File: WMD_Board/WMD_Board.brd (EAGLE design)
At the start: 65 x 45 mm, 60 parts, among them IC1 FGPMMOPA6H, J1 EMPCB.SMAFSTJ.B.HT, Q1 SI2323DS-T1-E3, U1 STM32L053C8T6, U2 BSS138, U3 RFM69HCW, U4 BSS138, U6 TPS72218DBVR, U7 M24512-DRMN8TP/K, Y2 ABS06-107-32.768KHZ-T

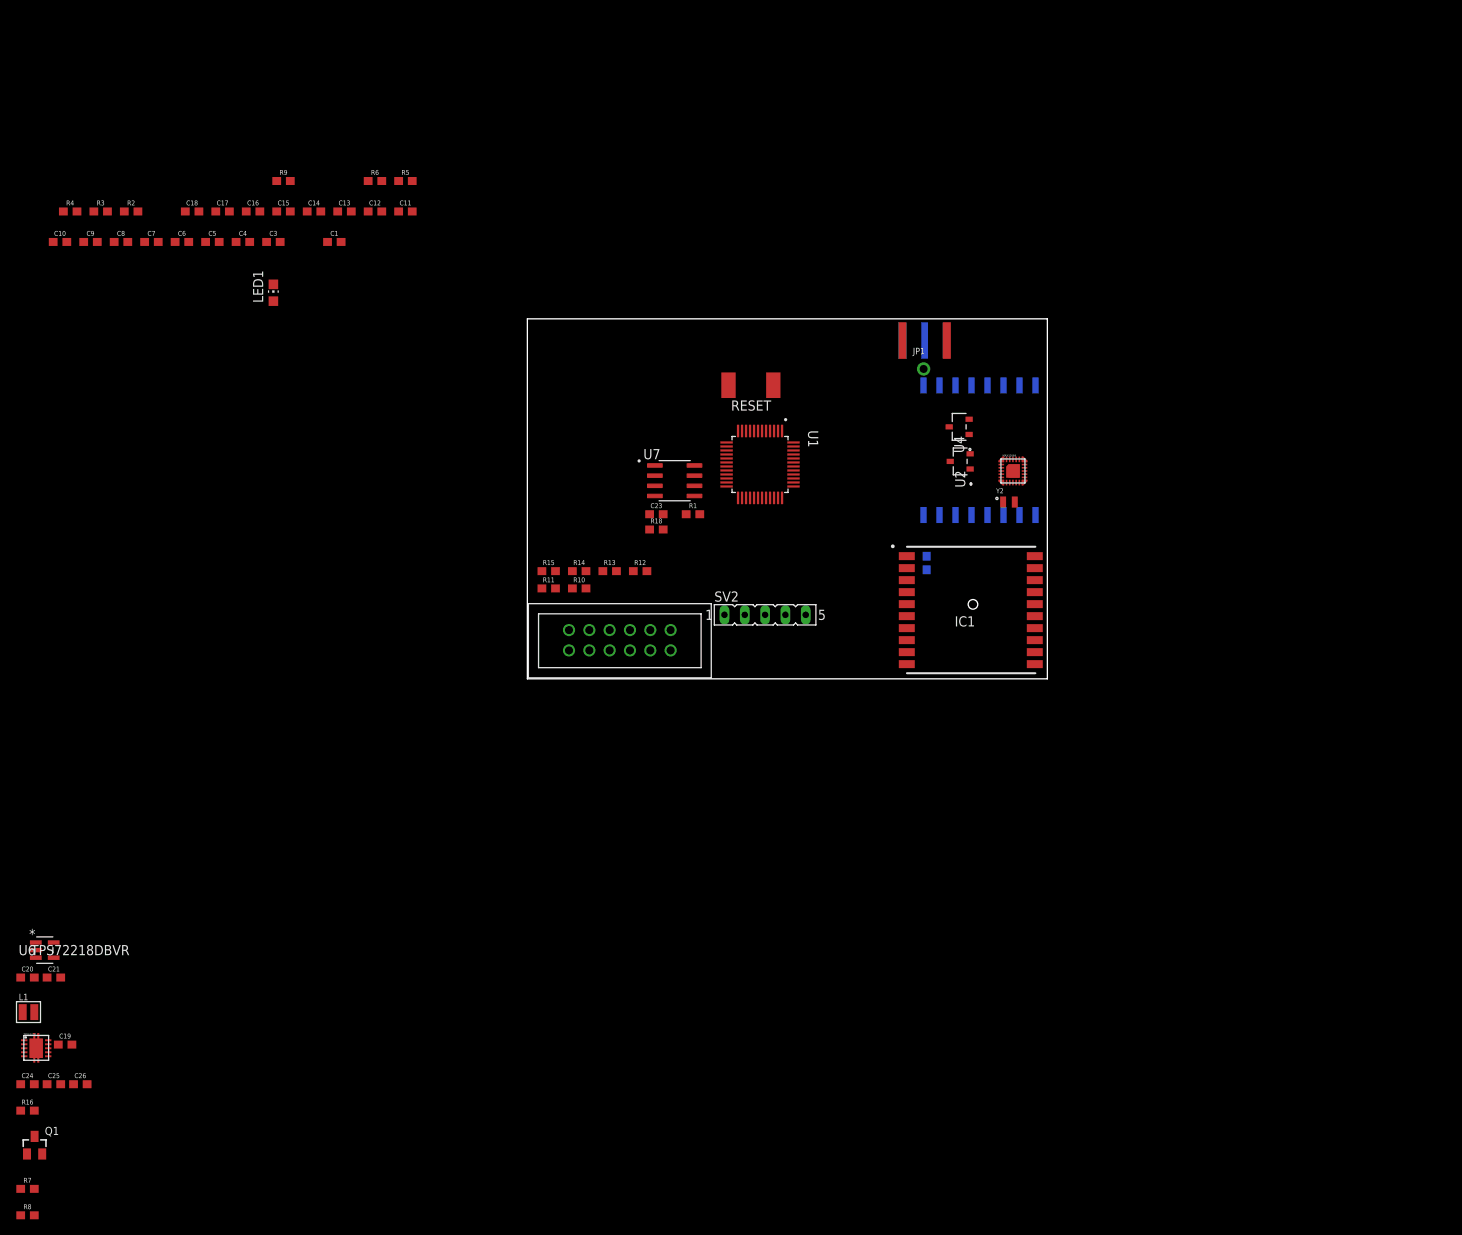
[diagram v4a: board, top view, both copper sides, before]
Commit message: Board routing started
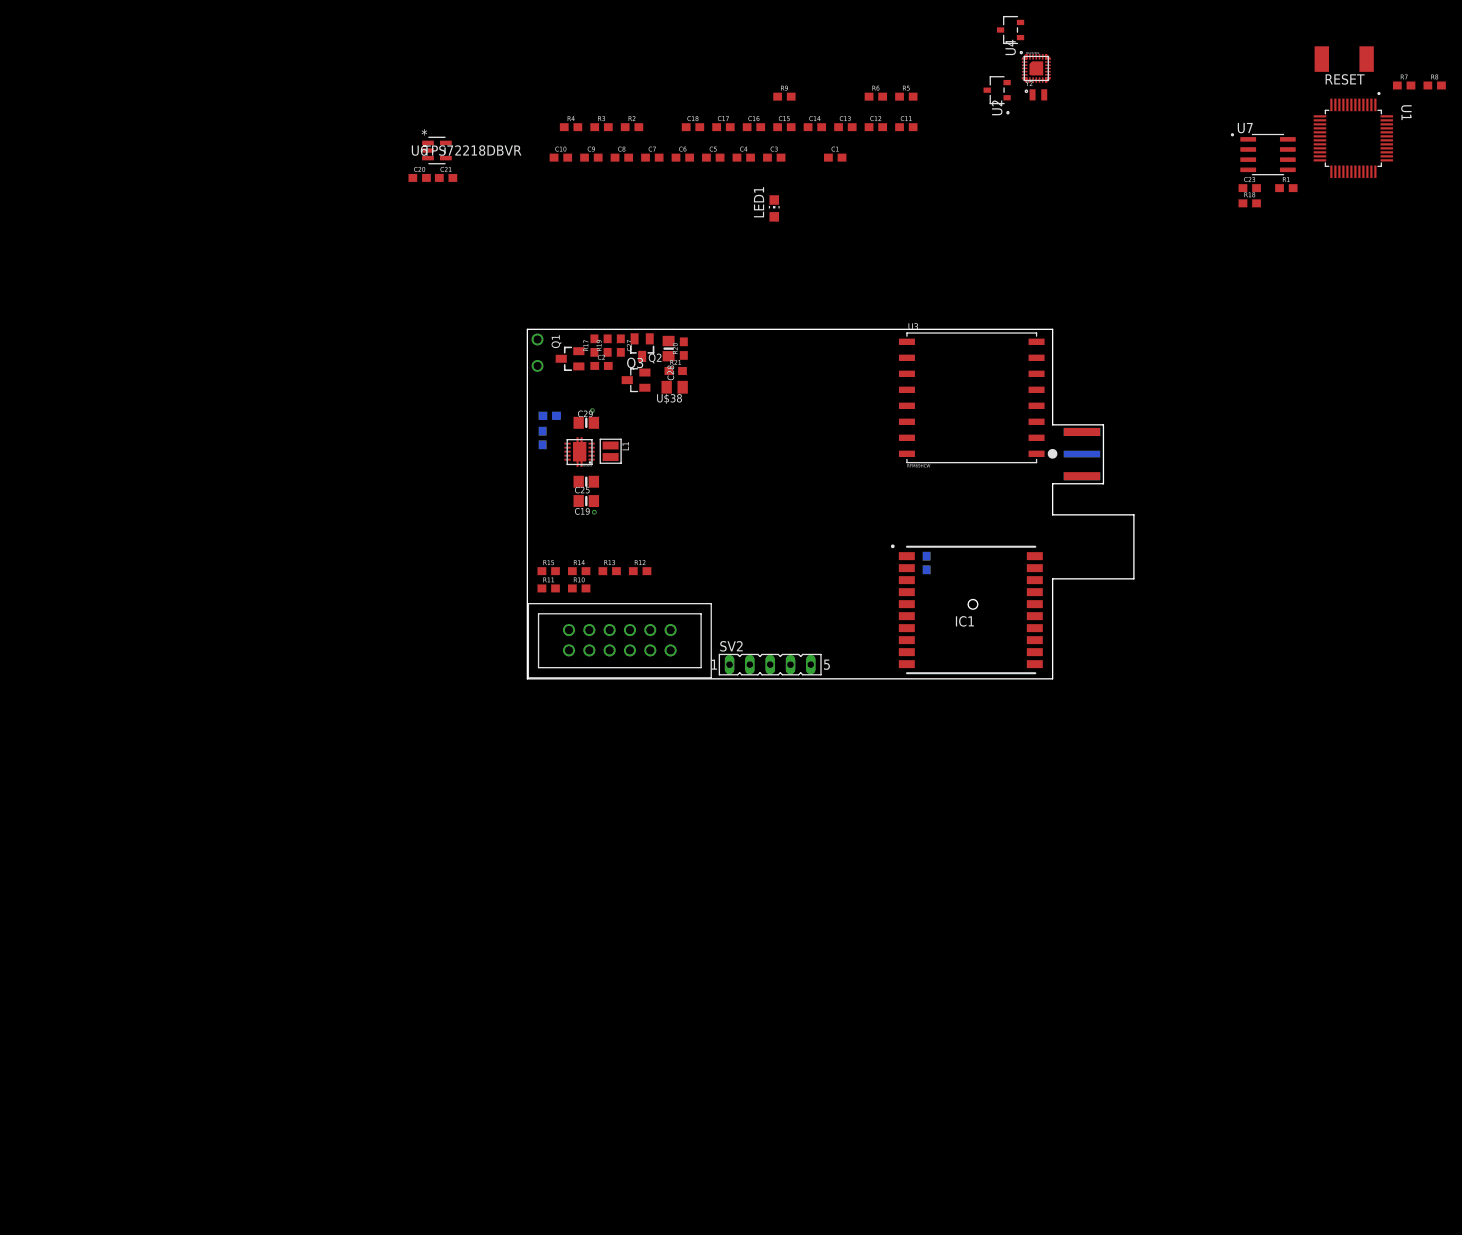
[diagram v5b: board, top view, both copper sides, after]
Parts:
- removed C24: 10uF, SparkFun-Capacitors:0603
- removed JP1: (no value), microbuilder:1X01_ROUND
- added C2, C27: 1.0uF, SparkFun-Capacitors:0603
- added C28, C29: 10uF, microbuilder:0805-NO
- added Q2: SI2323DS-T1-E3, SI2323DS-T1-E3:SOT23
- added Q3: SI2312BDS, SI2312BDS:SOT23
- added R17, R19, R20, R21: 1k, SparkFun-Resistors:0603
- added U$38: TS4148C_RZG, TS4148_RY:C0805K
- added U$40, U$41: BATTERY_HOLE, Battery_Hole:BATTERY_HOLE
- C11, C13, C18: value 1uF -> 1.0uF
- C14: value 100nF -> 1.0uF
- C17: value 0.1uF -> 4.7uF
- C19, C25: device SparkFun-Capacitors:0603 -> microbuilder:0805-NO
- C22: value 0.1uF -> 10uF
- R1, R18, R4, R5, R6, R9: value 4.7k -> 1k
- R16: value 100 -> 1k
- R3: value 10 -> 100k
- R7, R8: value 100k -> 1k
- moved R8 225.6 mm to (113.4, 74.2)
- moved R7 220.5 mm to (109.6, 74.2)
- moved Q1 118.9 mm to (5.33, 40.0), turned to 90 degrees
- moved U6 111.3 mm to (-11.3, 66.0)
- moved C20 111.3 mm to (-13.5, 62.6)
- moved C21 111.3 mm to (-10.2, 62.6)
- moved R16 108.7 mm to (2.79, 32.9), flipped to the bottom, turned to 180 degrees
- moved U$22 105.5 mm to (8.13, 30.1), turned to 180 degrees
- moved L1 101.0 mm to (10.4, 28.4), turned to 270 degrees
- moved C25 100.5 mm to (7.37, 24.6), turned to 180 degrees
- moved C26 99.3 mm to (1.91, 30.1), flipped to the bottom, turned to 270 degrees
- moved C19 94.1 mm to (7.37, 22.2), turned to 180 degrees
- moved R1 84.6 mm to (94.9, 61.3)
- moved RESET 84.6 mm to (102.1, 77.5)
- moved U1 84.6 mm to (103.3, 67.6)
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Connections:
- removed net V_BAT_MEASURE: R7.1
- new net MEASURE: C27.1, Q1.2, Q2.2, R17.2, R19.2, R7.1
- new net N$13: C28.2, Q3.1, R21.1
- new net N$14: C2.2, C27.2, Q2.1, Q3.3, R19.1
- new net SHUTDOWN: R20.1, R21.2, U$38.A, U1.2
- net 3.3V: now also C25.1; no longer C24.1
- net BTN_POWER_OUT: now also C2.1, R17.1, U$38.C
- net GND: now also C29.2, Q3.2, U$41.1; no longer C24.2
- net N$8: no longer JP1.1
- net VIN_BATTERY: now also U$40.1
- net VIN_BB: now also C28.1, C29.1, Q2.3, R20.2; no longer C25.1
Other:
- board size 65 x 45 mm -> 75.8 x 43.7 mm

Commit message: lots of routing stuff
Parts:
- added C24: 0.01uF, SparkFun-Capacitors:0603
- added C30: 0.1uF, SparkFun-Capacitors:0603
- added J2: 5015680607, WMD_TO_HRF:MOLEX_5015680607
- R4, R5, R6, R9: value 1k -> 4.7k
- moved RESET 125.4 mm to (-16.6, 37.2), turned to 0 degrees
- moved U1 101.9 mm to (12.1, 22.1)
- moved U7 99.7 mm to (3.43, 21.0), turned to 270 degrees
- moved U2 96.7 mm to (-16.9, 13.2)
- moved C20 93.2 mm to (79.3, 54.1), flipped to the bottom
- moved C21 92.7 mm to (81.8, 51.1), flipped to the bottom, turned to 90 degrees
- moved C23 92.0 mm to (4.06, 29.2), flipped to the bottom
- moved U6 91.7 mm to (79.2, 51.2), flipped to the bottom, turned to 90 degrees
- moved R5 87.5 mm to (-18.8, 15.6), turned to 270 degrees
- moved R1 81.8 mm to (20.7, 26.8), turned to 180 degrees
- moved R18 77.1 mm to (21.2, 25.3), turned to 180 degrees
- moved U4 73.0 mm to (40.5, 10.9)
- moved C5 64.3 mm to (13.7, 1.52), flipped to the bottom, turned to 180 degrees
- moved C4 63.5 mm to (2.29, 6.73), flipped to the bottom
- moved R6 63.3 mm to (36.8, 9.87)
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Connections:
- removed net BTN_2_2: C3.2
- removed net BTN_3_2: C4.2
- removed net BTN_4_2: C5.2
- net 1.8V: now also J2.1
- net 3.3V: now also C24.1, C30.1, J2.3
- net GND: now also C24.2, C3.2, C30.2, C4.2, C5.2, J2.6
- net INT: now also J2.2
- net SCL_TO_HR_SENSOR: now also J2.5
- net SDA_TO_HR_SENSOR: now also J2.4
- net WC_EEPROM: now also U1.20; no longer U1.46
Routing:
- net 3.3V: track 0.00 -> 19.6 mm, vias 0 -> 4
- net VIN_BB: track 0.00 -> 12.2 mm, vias 0 -> 2
- net N$14: track 0.00 -> 11.8 mm
- net MEASURE: track 0.00 -> 7.99 mm
- net N$13: track 0.00 -> 6.60 mm
- net N$8: track 0.00 -> 5.71 mm
- net GND: track 0.00 -> 5.06 mm
- net N$7: track 0.00 -> 4.76 mm
- net VIN_BATTERY: track 0.00 -> 4.22 mm
- net SHUTDOWN: track 0.00 -> 4.14 mm
- added copper zone on layer 1, net 3.3V
- added copper zone on layer 1, net GND
- added copper zone on layer 16, net GND
- added copper zone on layer 1, net N$2
- added copper zone on layer 1, net N$3
- added copper zone on layer 1, net VIN_BB
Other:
- board size 75.8 x 43.7 mm -> 75.7 x 43.7 mm

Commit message: lots of routing stuff
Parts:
- moved C30 1.27 mm to (35.4, 38.1)
- moved C24 1.27 mm to (37.0, 38.1)
- moved C19 1.02 mm to (32.8, 38.0)
- moved C25 0.51 mm to (30.9, 38.0)
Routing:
- net 3.3V: track 19.6 -> 18.3 mm
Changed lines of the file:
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@@
 <attribute name="VALUE" x="23.241" y="35.941" size="0.4064" layer="27" ratio="10" rot="R270"/>
 </element>
-<element name="C25" library="microbuilder" package="0805-NO" value="10uF" x="31.369" y="37.973" smashed="yes" rot="R270">
-<attribute name="NAME" x="32.004" y="38.481" size="0.8128" layer="25" ratio="18" rot="R270"/>
-<attribute name="VALUE" x="30.607" y="35.941" size="0.4064" layer="27" ratio="10" rot="R270"/>
-</element>
-<element name="C19" library="microbuilder" package="0805-NO" value="10uF" x="33.782" y="37.973" smashed="yes" rot="R270">
-<attribute name="NAME" x="34.671" y="38.481" size="0.8128" layer="25" ratio="18" rot="R270"/>
-<attribute name="VALUE" x="33.02" y="35.941" size="0.4064" layer="27" ratio="10" rot="R270"/>
-</element>
-<element name="C30" library="SparkFun-Capacitors" library_urn="urn:adsk.eagle:library:510" package="0603" package3d_urn="urn:adsk.eagle:package:37414/1" value="0.1uF" x="36.715" y="38.072" smashed="yes" rot="R270">
-<attribute name="NAME" x="37.477" y="38.072" size="0.6096" layer="25" font="vector" ratio="20" rot="R270" align="bottom-center"/>
-<attribute name="PROD_ID" value="CAP-00868" x="36.715" y="37.972" size="1.778" layer="27" rot="R270" display="off"/>
-<attribute name="VALUE" x="35.953" y="38.072" size="0.6096" layer="27" font="vector" ratio="20" rot="R270" align="top-center"/>
-</element>
-<element name="C24" library="SparkFun-Capacitors" library_urn="urn:adsk.eagle:library:510" package="0603" package3d_urn="urn:adsk.eagle:package:37414/1" value="0.01uF" x="38.227" y="38.0746" smashed="yes" rot="R270">
-<attribute name="NAME" x="38.989" y="38.0746" size="0.6096" layer="25" font="vector" ratio="20" rot="R270" align="bottom-center"/>
-<attribute name="PROD_ID" value="CAP-00868" x="38.227" y="37.9476" size="1.778" layer="27" rot="R270" display="off"/>
-<attribute name="VALUE" x="37.465" y="38.0746" size="0.6096" layer="27" font="vector" ratio="20" rot="R270" align="top-center"/>
+<element name="C25" library="microbuilder" package="0805-NO" value="10uF" x="30.861" y="37.973" smashed="yes" rot="R270">
+<attribute name="NAME" x="31.496" y="38.481" size="0.8128" layer="25" ratio="18" rot="R270"/>
+<attribute name="VALUE" x="30.099" y="35.941" size="0.4064" layer="27" ratio="10" rot="R270"/>
+</element>
+<element name="C19" library="microbuilder" package="0805-NO" value="10uF" x="32.766" y="37.973" smashed="yes" rot="R270">
+<attribute name="NAME" x="33.655" y="38.481" size="0.8128" layer="25" ratio="18" rot="R270"/>
+<attribute name="VALUE" x="32.004" y="35.941" size="0.4064" layer="27" ratio="10" rot="R270"/>
+</element>
+<element name="C30" library="SparkFun-Capacitors" library_urn="urn:adsk.eagle:library:510" package="0603" package3d_urn="urn:adsk.eagle:package:37414/1" value="0.1uF" x="35.445" y="38.072" smashed="yes" rot="R270">
+<attribute name="NAME" x="36.207" y="38.072" size="0.6096" layer="25" font="vector" ratio="20" rot="R270" align="bottom-center"/>
+<attribute name="PROD_ID" value="CAP-00868" x="35.445" y="37.972" size="1.778" layer="27" rot="R270" display="off"/>
+<attribute name="VALUE" x="34.683" y="38.072" size="0.6096" layer="27" font="vector" ratio="20" rot="R270" align="top-center"/>
+</element>
+<element name="C24" library="SparkFun-Capacitors" library_urn="urn:adsk.eagle:library:510" package="0603" package3d_urn="urn:adsk.eagle:package:37414/1" value="0.01uF" x="36.957" y="38.0746" smashed="yes" rot="R270">
+<attribute name="NAME" x="37.719" y="38.0746" size="0.6096" layer="25" font="vector" ratio="20" rot="R270" align="bottom-center"/>
+<attribute name="PROD_ID" value="CAP-00868" x="36.957" y="37.9476" size="1.778" layer="27" rot="R270" display="off"/>
+<attribute name="VALUE" x="36.195" y="38.0746" size="0.6096" layer="27" font="vector" ratio="20" rot="R270" align="top-center"/>
 </element>
 <element name="J2" library="WMD_TO_HRF" package="MOLEX_5015680607" value="5015680607" x="70.2564" y="15.6972" smashed="yes" rot="R90">
@@
 <polygon width="0.1524" layer="1" thermals="no">
 <vertex x="21.5392" y="37.8968"/>
-<vertex x="38.6842" y="37.8968"/>
-<vertex x="38.6842" y="36.2458"/>
+<vertex x="37.6682" y="37.8968"/>
+<vertex x="37.6682" y="36.2458"/>
 <vertex x="21.5392" y="36.2458"/>
 </polygon>
@@
 <contactref element="C5" pad="2"/>
 <polygon width="0.1524" layer="16" rank="4">
-<vertex x="46.482" y="43.688"/>
-<vertex x="46.482" y="26.924"/>
+<vertex x="45.212" y="43.688"/>
+<vertex x="45.212" y="26.924"/>
 <vertex x="65.659" y="26.924"/>
 <vertex x="65.659" y="24.384"/>
@@
 </polygon>
 <polygon width="0.1524" layer="1" rank="4">
-<vertex x="46.482" y="43.688"/>
-<vertex x="46.482" y="26.924"/>
+<vertex x="45.212" y="43.688"/>
+<vertex x="45.212" y="26.924"/>
 <vertex x="65.659" y="26.924"/>
 <vertex x="65.659" y="24.384"/>
@@
 <polygon width="0.1524" layer="1" rank="4">
 <vertex x="0" y="32.131"/>
-<vertex x="45.466" y="32.131"/>
-<vertex x="45.466" y="25.908"/>
+<vertex x="44.196" y="32.131"/>
+<vertex x="44.196" y="25.908"/>
 <vertex x="64.643" y="25.908"/>
 <vertex x="64.643" y="23.368"/>
@@
 <vertex x="64.643" y="23.368"/>
 <vertex x="64.643" y="25.908"/>
-<vertex x="45.466" y="25.908"/>
-<vertex x="45.466" y="32.131"/>
+<vertex x="44.196" y="25.908"/>
+<vertex x="44.196" y="32.131"/>
 </polygon>
 <wire x1="81.788" y1="51.9294" x2="114.261" y2="74.168" width="0" layer="19" extent="1-16"/>
@@
 <vertex x="28.5242" y="39.3192"/>
 <vertex x="28.5242" y="38.2016"/>
-<vertex x="38.6842" y="38.2016"/>
-<vertex x="38.6842" y="39.751"/>
+<vertex x="37.6682" y="38.2016"/>
+<vertex x="37.6682" y="39.751"/>
 <vertex x="29.3624" y="39.751"/>
 <vertex x="29.0576" y="39.4462"/>
 <vertex x="28.6512" y="39.4462"/>
 </polygon>
-<via x="35.4584" y="39.2938" extent="1-16" drill="0.35"/>
+<via x="34.1884" y="39.2938" extent="1-16" drill="0.35"/>
 <wire x1="28.608" y1="35.635" x2="28.608" y2="35.019" width="0.254" layer="1"/>
-<wire x1="28.608" y1="35.019" x2="28.8798" y2="34.7472" width="0.254" layer="1"/>
-<wire x1="28.8798" y1="34.7472" x2="34.6964" y2="34.7472" width="0.254" layer="1"/>
-<wire x1="34.6964" y1="34.7472" x2="35.4584" y2="35.5092" width="0.254" layer="1"/>
-<via x="35.4584" y="35.5092" extent="1-16" drill="0.35"/>
-<wire x1="35.4584" y1="35.5092" x2="35.4584" y2="39.2938" width="0.254" layer="16"/>
 <wire x1="47.43" y1="15.338" x2="49.628" y2="15.338" width="0.4064" layer="1"/>
 <wire x1="49.628" y1="15.338" x2="49.657" y2="15.367" width="0.4064" layer="1"/>
@@
 <contactref element="C24" pad="1"/>
 <contactref element="J2" pad="3"/>
+<wire x1="28.608" y1="35.019" x2="28.9306" y2="34.6964" width="0.254" layer="1"/>
+<wire x1="33.2994" y1="34.6964" x2="34.163" y2="35.56" width="0.254" layer="1"/>
+<via x="34.163" y="35.56" extent="1-16" drill="0.35"/>
+<wire x1="34.163" y1="35.56" x2="34.163" y2="39.2684" width="0.254" layer="16"/>
+<wire x1="34.163" y1="39.2684" x2="34.1884" y2="39.2938" width="0.254" layer="16"/>
+<wire x1="28.9306" y1="34.6964" x2="33.2994" y2="34.6964" width="0.254" layer="1"/>
 <wire x1="80.1472" y1="50.0634" x2="81.788" y2="50.2294" width="0" layer="19" extent="16-16"/>
 <wire x1="78.2472" y1="50.0634" x2="80.1472" y2="50.0634" width="0" layer="19" extent="16-16"/>
 <wire x1="63.6498" y1="36.1282" x2="78.2472" y2="50.0634" width="0" layer="19" extent="1-16"/>
-<wire x1="38.227" y1="38.9246" x2="59.761" y2="36.111" width="0" layer="19" extent="1-16"/>
-<wire x1="21.551" y1="26.797" x2="28.8798" y2="34.7472" width="0" layer="19" extent="1-1"/>
-<wire x1="22.059" y1="25.273" x2="21.551" y2="26.797" width="0" layer="19" extent="1-1"/>
+<wire x1="70.2564" y1="15.1972" x2="63.6498" y2="36.1282" width="0" layer="19" extent="1-1"/>
+<wire x1="51.308" y1="15.328" x2="70.2564" y2="15.1972" width="0" layer="19" extent="1-16"/>
+<wire x1="35.781" y1="11.871" x2="47.43" y2="15.338" width="0" layer="19" extent="1-1"/>
+<wire x1="35.433" y1="1.778" x2="35.781" y2="11.871" width="0" layer="19" extent="1-1"/>
+<wire x1="22.059" y1="25.273" x2="35.781" y2="11.871" width="0" layer="19" extent="1-1"/>
+<wire x1="21.551" y1="26.797" x2="22.059" y2="25.273" width="0" layer="19" extent="1-1"/>
 <wire x1="16.245" y1="24.848" x2="21.551" y2="26.797" width="0" layer="19" extent="1-1"/>
 <wire x1="13.931" y1="24.638" x2="16.201" y2="24.892" width="0" layer="19" extent="1-16"/>
@@
 <wire x1="6.008" y1="1.524" x2="1.436" y2="3.429" width="0" layer="19" extent="16-16"/>
 <wire x1="15.367" y1="3.556" x2="6.008" y2="1.524" width="0" layer="19" extent="16-16"/>
-<wire x1="35.781" y1="11.871" x2="22.059" y2="25.273" width="0" layer="19" extent="1-1"/>
-<wire x1="35.433" y1="1.778" x2="35.781" y2="11.871" width="0" layer="19" extent="1-1"/>
-<wire x1="47.43" y1="15.338" x2="35.781" y2="11.871" width="0" layer="19" extent="1-1"/>
-<wire x1="70.2564" y1="15.1972" x2="51.308" y2="15.328" width="0" layer="19" extent="1-16"/>
+<wire x1="28.9306" y1="34.6964" x2="21.551" y2="26.797" width="0" layer="19" extent="1-1"/>
 <wire x1="-18.841" y1="16.427" x2="1.436" y2="3.429" width="0" layer="19" extent="1-16"/>
 </signal>

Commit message: noise snubber
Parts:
- C14: value 1.0uF -> 100nF
- R3: value 100k -> 10
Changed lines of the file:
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@@
 <attribute name="VALUE" x="39.751" y="68.199" size="0.6096" layer="27" font="vector" ratio="20" align="top-center"/>
 </element>
-<element name="C14" library="SparkFun-Capacitors" package="0603" value="1.0uF" x="35.941" y="68.961" smashed="yes">
+<element name="C14" library="SparkFun-Capacitors" package="0603" value="100nF" x="35.941" y="68.961" smashed="yes">
 <attribute name="NAME" x="35.941" y="69.723" size="0.6096" layer="25" font="vector" ratio="20" align="bottom-center"/>
 <attribute name="PROD_ID" value="CAP-00868" x="35.941" y="68.961" size="1.778" layer="27" display="off"/>
@@
 <attribute name="VALUE" x="13.081" y="68.199" size="0.6096" layer="27" font="vector" ratio="20" align="top-center"/>
 </element>
-<element name="R3" library="SparkFun-Resistors" package="0603" value="100k" x="9.271" y="68.961" smashed="yes">
+<element name="R3" library="SparkFun-Resistors" package="0603" value="10" x="9.271" y="68.961" smashed="yes">
 <attribute name="NAME" x="9.271" y="69.723" size="0.6096" layer="25" font="vector" ratio="20" align="bottom-center"/>
 <attribute name="PROD_ID" value="RES-07828" x="9.271" y="68.961" size="1.778" layer="27" display="off"/>
